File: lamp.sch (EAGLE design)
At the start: 42 parts

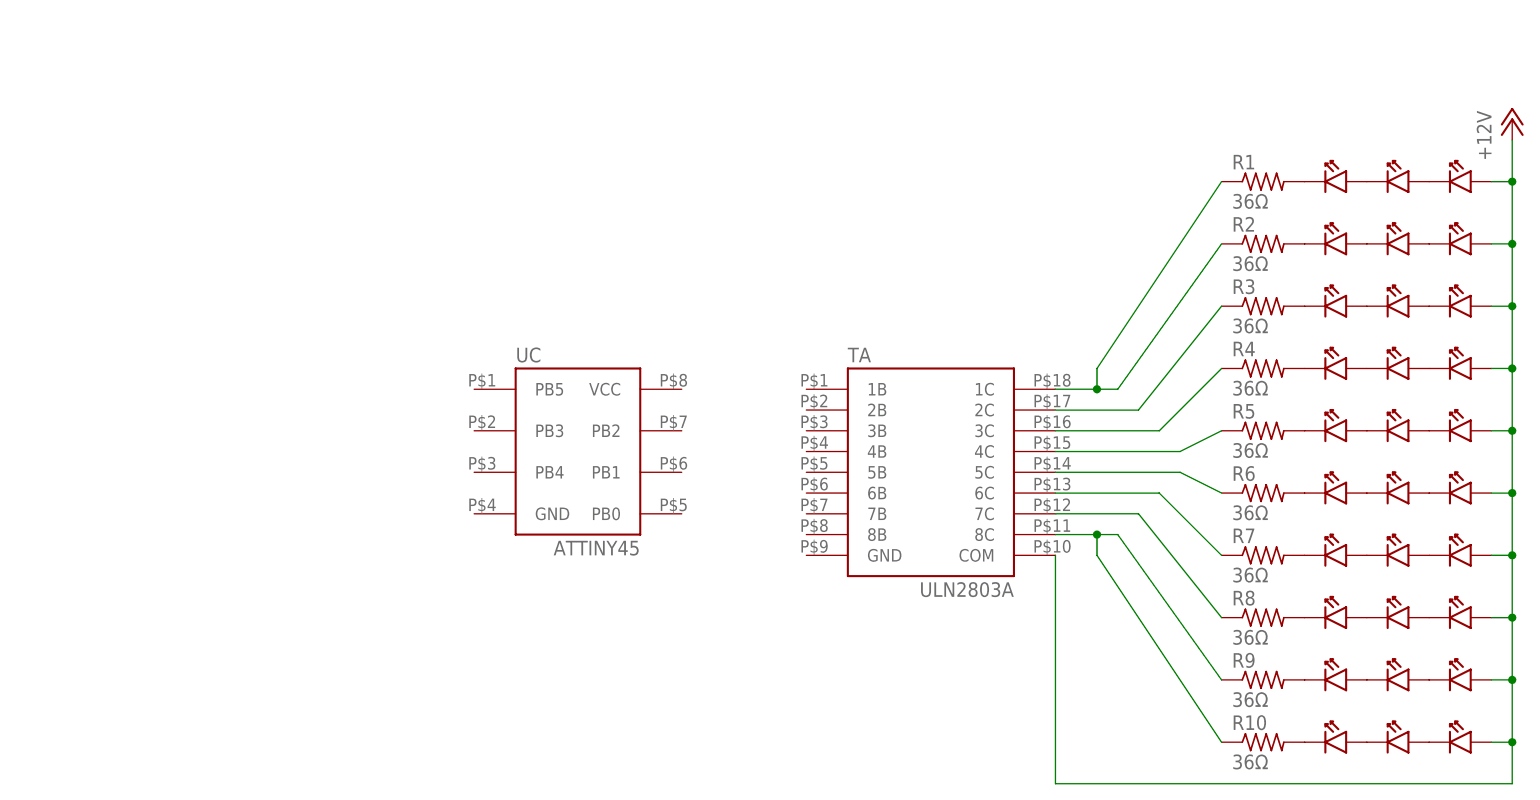
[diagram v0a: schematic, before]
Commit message: Added power supply for microcontroller, more routing, and some minor rearrangement on parts. Added solder pads for controller. Added ground plane for bottom.
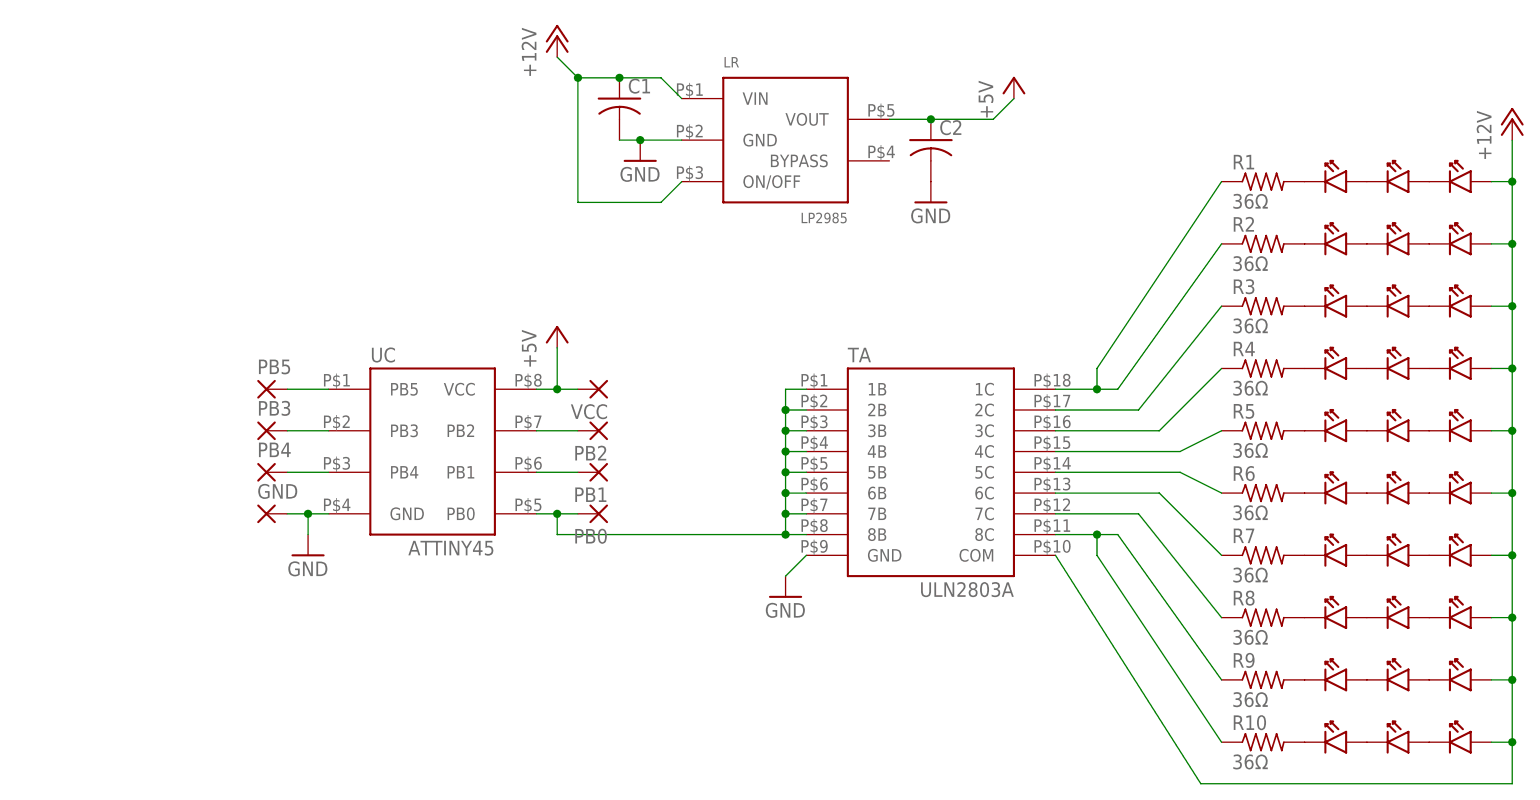
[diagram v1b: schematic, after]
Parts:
- removed U$19: CLA1BWKWMKW-4, lamp:CLA1BWKWMKW-4
- added C1, C2: (no value), Barebones-Arduino:CAPACITOR-SMD
- added GND, PB0, PB1, PB2, PB3, PB4, PB5, VCC: (no value), wirepad:SMD2
- added LR: LP2985, lamp:LP2985
- added U$1: CLA1BWKWMKW-4, lamp:CLA1BWKWMKW-4
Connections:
- new net GND: C1.2, C2.2, GND.P, LR.GND, TA.GND, UC.GND
- new net N$13: R6.2, U$18.P$2
- new net N$16: U$16.P$2, U$17.P$1
- new net N$31: U$1.P$2, U$14.P$1
- new net N$39: PB3.P, UC.PB3
- new net N$43: R5.2, U$15.P$2
- new net N$44: PB4.P, UC.PB4
- new net N$47: PB0.P, TA.1B, TA.2B, TA.3B, TA.4B, TA.5B, TA.6B, TA.7B, TA.8B, UC.PB0
- net +12V: now also C1.1, LR.ON/OFF, LR.VIN, U$1.P$1, U$16.P$1; no longer U$14.P$1, U$17.P$1
- net N$14: now also PB1.P, UC.PB1; no longer R5.2, U$16.P$2
- net N$15: now also C2.1, LR.VOUT, UC.VCC, VCC.P; no longer U$15.P$2, U$16.P$1
- net N$17: now also PB2.P, UC.PB2; no longer R6.2, U$19.P$2
- net N$18: now also PB5.P, UC.PB5; no longer U$18.P$2, U$19.P$1
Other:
- moved on the sheet: UC

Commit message: Finished top layer: added heat sink flags on the leds, filled in the ground plane, did some more routing. Because I'm on babby's first eagle license, I can't place the last 8 parts, but all the routing at that end is done and the parts are space correctly relative to each other, they just need to be move into place as a single group.
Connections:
- net +12V: now also U$1.P$2, U$11.P$2, U$16.P$2, U$2.P$2, U$20.P$2, U$23.P$2, U$26.P$2, U$29.P$2, U$5.P$2, U$8.P$2; no longer U$1.P$1, U$11.P$1, U$16.P$1, U$2.P$1, U$20.P$1, U$23.P$1, U$26.P$1, U$29.P$1, U$5.P$1, U$8.P$1
- net N$1: now also U$2.P$4, U$3.P$2; no longer U$2.P$2, U$3.P$1
- net N$10: now also U$11.P$4, U$12.P$2; no longer U$11.P$2, U$12.P$1
- net N$11: now also U$13.P$4; no longer U$13.P$2
- net N$12: now also U$12.P$4, U$13.P$2; no longer U$12.P$2, U$13.P$1
- net N$13: now also U$18.P$4; no longer U$18.P$2
- net N$16: now also U$16.P$4, U$17.P$2; no longer U$16.P$2, U$17.P$1
- net N$19: now also U$20.P$4, U$21.P$2; no longer U$20.P$2, U$21.P$1
- net N$2: now also U$4.P$4; no longer U$4.P$2
- net N$20: now also U$22.P$4; no longer U$22.P$2
- net N$21: now also U$21.P$4, U$22.P$2; no longer U$21.P$2, U$22.P$1
- net N$22: now also U$23.P$4, U$24.P$2; no longer U$23.P$2, U$24.P$1
- net N$23: now also U$25.P$4; no longer U$25.P$2
- net N$24: now also U$24.P$4, U$25.P$2; no longer U$24.P$2, U$25.P$1
- net N$25: now also U$26.P$4, U$27.P$2; no longer U$26.P$2, U$27.P$1
- net N$26: now also U$28.P$4; no longer U$28.P$2
- net N$27: now also U$27.P$4, U$28.P$2; no longer U$27.P$2, U$28.P$1
- net N$28: now also U$29.P$4, U$30.P$2; no longer U$29.P$2, U$30.P$1
- net N$29: now also U$31.P$4; no longer U$31.P$2
- net N$3: now also U$3.P$4, U$4.P$2; no longer U$3.P$2, U$4.P$1
- net N$30: now also U$30.P$4, U$31.P$2; no longer U$30.P$2, U$31.P$1
- net N$31: now also U$1.P$4, U$14.P$2; no longer U$1.P$2, U$14.P$1
- net N$32: now also U$14.P$4, U$15.P$2; no longer U$14.P$2, U$15.P$1
- net N$4: now also U$5.P$4, U$6.P$2; no longer U$5.P$2, U$6.P$1
- net N$40: now also U$17.P$4, U$18.P$2; no longer U$17.P$2, U$18.P$1
- net N$43: now also U$15.P$4; no longer U$15.P$2
- net N$5: now also U$7.P$4; no longer U$7.P$2
- net N$6: now also U$6.P$4, U$7.P$2; no longer U$6.P$2, U$7.P$1
- net N$7: now also U$8.P$4, U$9.P$2; no longer U$8.P$2, U$9.P$1
- net N$8: now also U$10.P$4; no longer U$10.P$2
- net N$9: now also U$10.P$2, U$9.P$4; no longer U$10.P$1, U$9.P$2
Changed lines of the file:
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@@
 <net name="N$1" class="0">
 <segment>
-<pinref part="U$2" gate="G$1" pin="P$2"/>
-<pinref part="U$3" gate="G$1" pin="P$1"/>
+<pinref part="U$2" gate="G$1" pin="P$4"/>
+<pinref part="U$3" gate="G$1" pin="P$2"/>
 </segment>
 </net>
@@
 <segment>
 <pinref part="R1" gate="G$1" pin="2"/>
+<pinref part="U$4" gate="G$1" pin="P$4"/>
+</segment>
+</net>
+<net name="N$3" class="0">
+<segment>
+<pinref part="U$3" gate="G$1" pin="P$4"/>
 <pinref part="U$4" gate="G$1" pin="P$2"/>
 </segment>
 </net>
-<net name="N$3" class="0">
-<segment>
-<pinref part="U$3" gate="G$1" pin="P$2"/>
-<pinref part="U$4" gate="G$1" pin="P$1"/>
-</segment>
-</net>
 <net name="N$4" class="0">
 <segment>
-<pinref part="U$5" gate="G$1" pin="P$2"/>
-<pinref part="U$6" gate="G$1" pin="P$1"/>
+<pinref part="U$5" gate="G$1" pin="P$4"/>
+<pinref part="U$6" gate="G$1" pin="P$2"/>
 </segment>
 </net>
@@
 <segment>
 <pinref part="R2" gate="G$1" pin="2"/>
+<pinref part="U$7" gate="G$1" pin="P$4"/>
+</segment>
+</net>
+<net name="N$6" class="0">
+<segment>
+<pinref part="U$6" gate="G$1" pin="P$4"/>
 <pinref part="U$7" gate="G$1" pin="P$2"/>
 </segment>
 </net>
-<net name="N$6" class="0">
-<segment>
-<pinref part="U$6" gate="G$1" pin="P$2"/>
-<pinref part="U$7" gate="G$1" pin="P$1"/>
-</segment>
-</net>
 <net name="N$7" class="0">
 <segment>
-<pinref part="U$8" gate="G$1" pin="P$2"/>
-<pinref part="U$9" gate="G$1" pin="P$1"/>
+<pinref part="U$8" gate="G$1" pin="P$4"/>
+<pinref part="U$9" gate="G$1" pin="P$2"/>
 </segment>
 </net>
@@
 <segment>
 <pinref part="R3" gate="G$1" pin="2"/>
+<pinref part="U$10" gate="G$1" pin="P$4"/>
+</segment>
+</net>
+<net name="N$9" class="0">
+<segment>
+<pinref part="U$9" gate="G$1" pin="P$4"/>
 <pinref part="U$10" gate="G$1" pin="P$2"/>
 </segment>
 </net>
-<net name="N$9" class="0">
-<segment>
-<pinref part="U$9" gate="G$1" pin="P$2"/>
-<pinref part="U$10" gate="G$1" pin="P$1"/>
-</segment>
-</net>
 <net name="N$10" class="0">
 <segment>
-<pinref part="U$11" gate="G$1" pin="P$2"/>
-<pinref part="U$12" gate="G$1" pin="P$1"/>
+<pinref part="U$11" gate="G$1" pin="P$4"/>
+<pinref part="U$12" gate="G$1" pin="P$2"/>
 </segment>
 </net>
@@
 <segment>
 <pinref part="R4" gate="G$1" pin="2"/>
+<pinref part="U$13" gate="G$1" pin="P$4"/>
+</segment>
+</net>
+<net name="N$12" class="0">
+<segment>
+<pinref part="U$12" gate="G$1" pin="P$4"/>
 <pinref part="U$13" gate="G$1" pin="P$2"/>
 </segment>
 </net>
-<net name="N$12" class="0">
-<segment>
-<pinref part="U$12" gate="G$1" pin="P$2"/>
-<pinref part="U$13" gate="G$1" pin="P$1"/>
-</segment>
-</net>
 <net name="N$19" class="0">
 <segment>
-<pinref part="U$20" gate="G$1" pin="P$2"/>
-<pinref part="U$21" gate="G$1" pin="P$1"/>
+<pinref part="U$20" gate="G$1" pin="P$4"/>
+<pinref part="U$21" gate="G$1" pin="P$2"/>
 </segment>
 </net>
@@
 <segment>
 <pinref part="R7" gate="G$1" pin="2"/>
+<pinref part="U$22" gate="G$1" pin="P$4"/>
+</segment>
+</net>
+<net name="N$21" class="0">
+<segment>
+<pinref part="U$21" gate="G$1" pin="P$4"/>
 <pinref part="U$22" gate="G$1" pin="P$2"/>
 </segment>
 </net>
-<net name="N$21" class="0">
-<segment>
-<pinref part="U$21" gate="G$1" pin="P$2"/>
-<pinref part="U$22" gate="G$1" pin="P$1"/>
-</segment>
-</net>
 <net name="N$22" class="0">
 <segment>
-<pinref part="U$23" gate="G$1" pin="P$2"/>
-<pinref part="U$24" gate="G$1" pin="P$1"/>
+<pinref part="U$23" gate="G$1" pin="P$4"/>
+<pinref part="U$24" gate="G$1" pin="P$2"/>
 </segment>
 </net>
@@
 <segment>
 <pinref part="R8" gate="G$1" pin="2"/>
+<pinref part="U$25" gate="G$1" pin="P$4"/>
+</segment>
+</net>
+<net name="N$24" class="0">
+<segment>
+<pinref part="U$24" gate="G$1" pin="P$4"/>
 <pinref part="U$25" gate="G$1" pin="P$2"/>
 </segment>
 </net>
-<net name="N$24" class="0">
-<segment>
-<pinref part="U$24" gate="G$1" pin="P$2"/>
-<pinref part="U$25" gate="G$1" pin="P$1"/>
-</segment>
-</net>
 <net name="N$25" class="0">
 <segment>
-<pinref part="U$26" gate="G$1" pin="P$2"/>
-<pinref part="U$27" gate="G$1" pin="P$1"/>
+<pinref part="U$26" gate="G$1" pin="P$4"/>
+<pinref part="U$27" gate="G$1" pin="P$2"/>
 </segment>
 </net>
@@
 <segment>
 <pinref part="R9" gate="G$1" pin="2"/>
+<pinref part="U$28" gate="G$1" pin="P$4"/>
+</segment>
+</net>
+<net name="N$27" class="0">
+<segment>
+<pinref part="U$27" gate="G$1" pin="P$4"/>
 <pinref part="U$28" gate="G$1" pin="P$2"/>
 </segment>
 </net>
-<net name="N$27" class="0">
-<segment>
-<pinref part="U$27" gate="G$1" pin="P$2"/>
-<pinref part="U$28" gate="G$1" pin="P$1"/>
-</segment>
-</net>
 <net name="N$28" class="0">
 <segment>
-<pinref part="U$29" gate="G$1" pin="P$2"/>
-<pinref part="U$30" gate="G$1" pin="P$1"/>
+<pinref part="U$29" gate="G$1" pin="P$4"/>
+<pinref part="U$30" gate="G$1" pin="P$2"/>
 </segment>
 </net>
@@
 <segment>
 <pinref part="R10" gate="G$1" pin="2"/>
+<pinref part="U$31" gate="G$1" pin="P$4"/>
+</segment>
+</net>
+<net name="N$30" class="0">
+<segment>
+<pinref part="U$30" gate="G$1" pin="P$4"/>
 <pinref part="U$31" gate="G$1" pin="P$2"/>
-</segment>
-</net>
-<net name="N$30" class="0">
-<segment>
-<pinref part="U$30" gate="G$1" pin="P$2"/>
-<pinref part="U$31" gate="G$1" pin="P$1"/>
 </segment>
 </net>
@@
 <wire x1="132.08" y1="7.62" x2="134.62" y2="7.62" width="0.1524" layer="91"/>
 <junction x="134.62" y="7.62"/>
-<pinref part="U$2" gate="G$1" pin="P$1"/>
-<pinref part="U$5" gate="G$1" pin="P$1"/>
-<pinref part="U$8" gate="G$1" pin="P$1"/>
-<pinref part="U$11" gate="G$1" pin="P$1"/>
-<pinref part="U$20" gate="G$1" pin="P$1"/>
-<pinref part="U$23" gate="G$1" pin="P$1"/>
-<pinref part="U$26" gate="G$1" pin="P$1"/>
-<pinref part="U$29" gate="G$1" pin="P$1"/>
+<pinref part="U$2" gate="G$1" pin="P$2"/>
+<pinref part="U$5" gate="G$1" pin="P$2"/>
+<pinref part="U$8" gate="G$1" pin="P$2"/>
+<pinref part="U$11" gate="G$1" pin="P$2"/>
+<pinref part="U$20" gate="G$1" pin="P$2"/>
+<pinref part="U$23" gate="G$1" pin="P$2"/>
+<pinref part="U$26" gate="G$1" pin="P$2"/>
+<pinref part="U$29" gate="G$1" pin="P$2"/>
 <pinref part="P+1" gate="1" pin="+12V"/>
 <wire x1="134.62" y1="81.28" x2="134.62" y2="76.2" width="0.1524" layer="91"/>
 <junction x="134.62" y="76.2"/>
-<pinref part="U$1" gate="G$1" pin="P$1"/>
-<pinref part="U$16" gate="G$1" pin="P$1"/>
+<pinref part="U$1" gate="G$1" pin="P$2"/>
+<pinref part="U$16" gate="G$1" pin="P$2"/>
 </segment>
 <segment>
@@
 <net name="N$31" class="0">
 <segment>
-<pinref part="U$1" gate="G$1" pin="P$2"/>
-<pinref part="U$14" gate="G$1" pin="P$1"/>
+<pinref part="U$1" gate="G$1" pin="P$4"/>
+<pinref part="U$14" gate="G$1" pin="P$2"/>
 </segment>
 </net>
 <net name="N$32" class="0">
 <segment>
-<pinref part="U$14" gate="G$1" pin="P$2"/>
-<pinref part="U$15" gate="G$1" pin="P$1"/>
+<pinref part="U$14" gate="G$1" pin="P$4"/>
+<pinref part="U$15" gate="G$1" pin="P$2"/>
 </segment>
 </net>
 <net name="N$16" class="0">
 <segment>
-<pinref part="U$16" gate="G$1" pin="P$2"/>
-<pinref part="U$17" gate="G$1" pin="P$1"/>
+<pinref part="U$16" gate="G$1" pin="P$4"/>
+<pinref part="U$17" gate="G$1" pin="P$2"/>
 </segment>
 </net>
 <net name="N$40" class="0">
 <segment>
-<pinref part="U$17" gate="G$1" pin="P$2"/>
-<pinref part="U$18" gate="G$1" pin="P$1"/>
+<pinref part="U$17" gate="G$1" pin="P$4"/>
+<pinref part="U$18" gate="G$1" pin="P$2"/>
 </segment>
 </net>
@@
 <net name="N$43" class="0">
 <segment>
-<pinref part="U$15" gate="G$1" pin="P$2"/>
+<pinref part="U$15" gate="G$1" pin="P$4"/>
 <pinref part="R5" gate="G$1" pin="2"/>
 </segment>
@@
 <net name="N$13" class="0">
 <segment>
-<pinref part="U$18" gate="G$1" pin="P$2"/>
+<pinref part="U$18" gate="G$1" pin="P$4"/>
 <pinref part="R6" gate="G$1" pin="2"/>
 </segment>

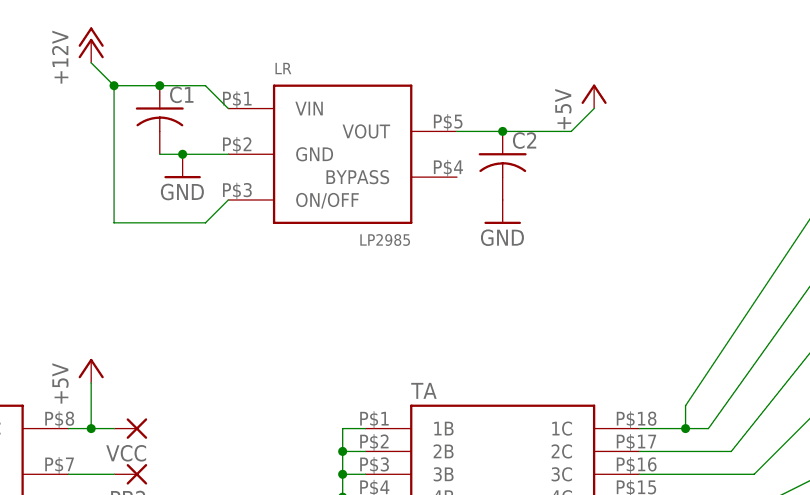
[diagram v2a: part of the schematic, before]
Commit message: Fiddled the board xml by hand to place the last few parts. Some more adjustment of traces. Added a low-noise cap to the 5v regulator.
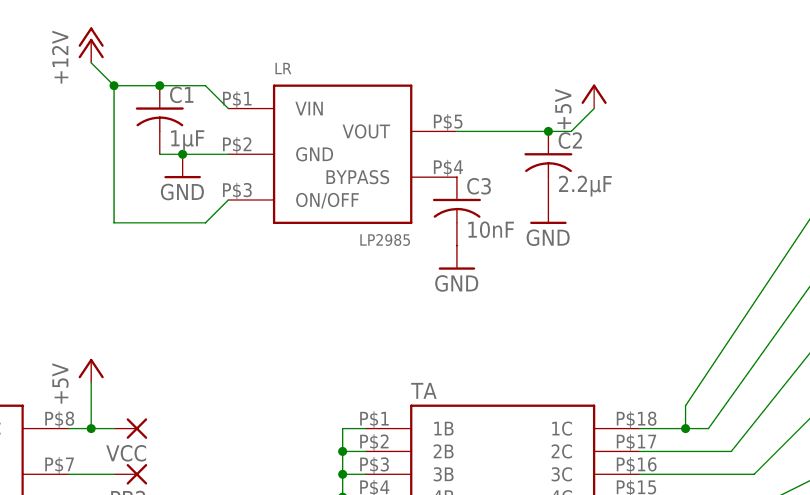
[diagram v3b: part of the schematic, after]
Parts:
- added C3: 10nF, Barebones-Arduino:CAPACITOR-SMD
- C1: value (none) -> 1µF
- C2: value (none) -> 2.2µF
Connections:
- new net N$46: C3.1, LR.BYPASS
- net GND: now also C3.2
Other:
- moved on the sheet: C2
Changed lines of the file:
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@@
 <part name="GND5" library=" Barebones-Arduino" deviceset="GND" device=""/>
 <part name="LR" library="lamp" deviceset="LP2985" device=""/>
-<part name="C1" library=" Barebones-Arduino" deviceset="CAPACITOR" device="-SMD"/>
-<part name="C2" library=" Barebones-Arduino" deviceset="CAPACITOR" device="-SMD"/>
+<part name="C1" library=" Barebones-Arduino" deviceset="CAPACITOR" device="-SMD" value="1µF"/>
+<part name="C2" library=" Barebones-Arduino" deviceset="CAPACITOR" device="-SMD" value="2.2µF"/>
 <part name="P+4" library=" Barebones-Arduino" deviceset="+5V" device=""/>
 <part name="PB1" library="wirepad" deviceset="SMD2" device=""/>
@@
 <part name="VCC" library="wirepad" deviceset="SMD2" device=""/>
 <part name="GND" library="wirepad" deviceset="SMD2" device=""/>
+<part name="C3" library=" Barebones-Arduino" deviceset="CAPACITOR" device="-SMD" value="10nF"/>
+<part name="GND4" library=" Barebones-Arduino" deviceset="GND" device=""/>
 </parts>
 <sheets>
@@
 <instance part="GND2" gate="1" x="-12.7" y="30.48"/>
 <instance part="P+2" gate="1" x="17.78" y="58.42"/>
-<instance part="GND3" gate="1" x="63.5" y="73.66"/>
+<instance part="GND3" gate="1" x="68.58" y="73.66"/>
 <instance part="P+3" gate="1" x="17.78" y="93.98"/>
 <instance part="GND5" gate="1" x="27.94" y="78.74"/>
 <instance part="LR" gate="G$1" x="45.72" y="81.28"/>
 <instance part="C1" gate="G$1" x="25.4" y="86.36"/>
-<instance part="C2" gate="G$1" x="63.5" y="81.28"/>
+<instance part="C2" gate="G$1" x="68.58" y="81.28"/>
 <instance part="P+4" gate="1" x="73.66" y="88.9"/>
 <instance part="PB1" gate="1" x="22.86" y="40.64" rot="R180"/>
@@
 <instance part="VCC" gate="1" x="22.86" y="50.8" rot="R180"/>
 <instance part="GND" gate="1" x="-17.78" y="35.56"/>
+<instance part="C3" gate="G$1" x="58.42" y="76.2"/>
+<instance part="GND4" gate="1" x="58.42" y="68.58"/>
 </instances>
 <busses>
@@
 <junction x="-12.7" y="35.56"/>
 </segment>
+<segment>
+<pinref part="C3" gate="G$1" pin="2"/>
+<pinref part="GND4" gate="1" pin="GND"/>
+</segment>
 </net>
 <net name="N$15" class="0">
@@
 <pinref part="LR" gate="G$1" pin="VOUT"/>
 <pinref part="C2" gate="G$1" pin="1"/>
-<wire x1="58.42" y1="83.82" x2="63.5" y2="83.82" width="0.1524" layer="91"/>
-<junction x="63.5" y="83.82"/>
-<wire x1="71.12" y1="83.82" x2="63.5" y2="83.82" width="0.1524" layer="91"/>
+<wire x1="58.42" y1="83.82" x2="68.58" y2="83.82" width="0.1524" layer="91"/>
+<junction x="68.58" y="83.82"/>
+<wire x1="71.12" y1="83.82" x2="68.58" y2="83.82" width="0.1524" layer="91"/>
 </segment>
 <segment>
@@
 </segment>
 </net>
+<net name="N$46" class="0">
+<segment>
+<pinref part="LR" gate="G$1" pin="BYPASS"/>
+<pinref part="C3" gate="G$1" pin="1"/>
+</segment>
+</net>
